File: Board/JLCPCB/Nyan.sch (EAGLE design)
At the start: 64 parts, among them Q1 8M, Q2 32768, U1 R-78C5.0-1.0, U3 A4988_STEP, U4 MAX6966, U5 ST3485, U6 74HCT541PW, U7 74HCT541PW, U8 STM32F10XCXT6, X1 WR-WTB2.0-2_THT-VER, X2 WR-WTB2.0-4_THT_VER, X3 WR-WTB2.0-5_THT-VER, X4 WR-WTB2.0-5_THT-VER, X6 68610614122, X7 68612414422, X8 68610414122

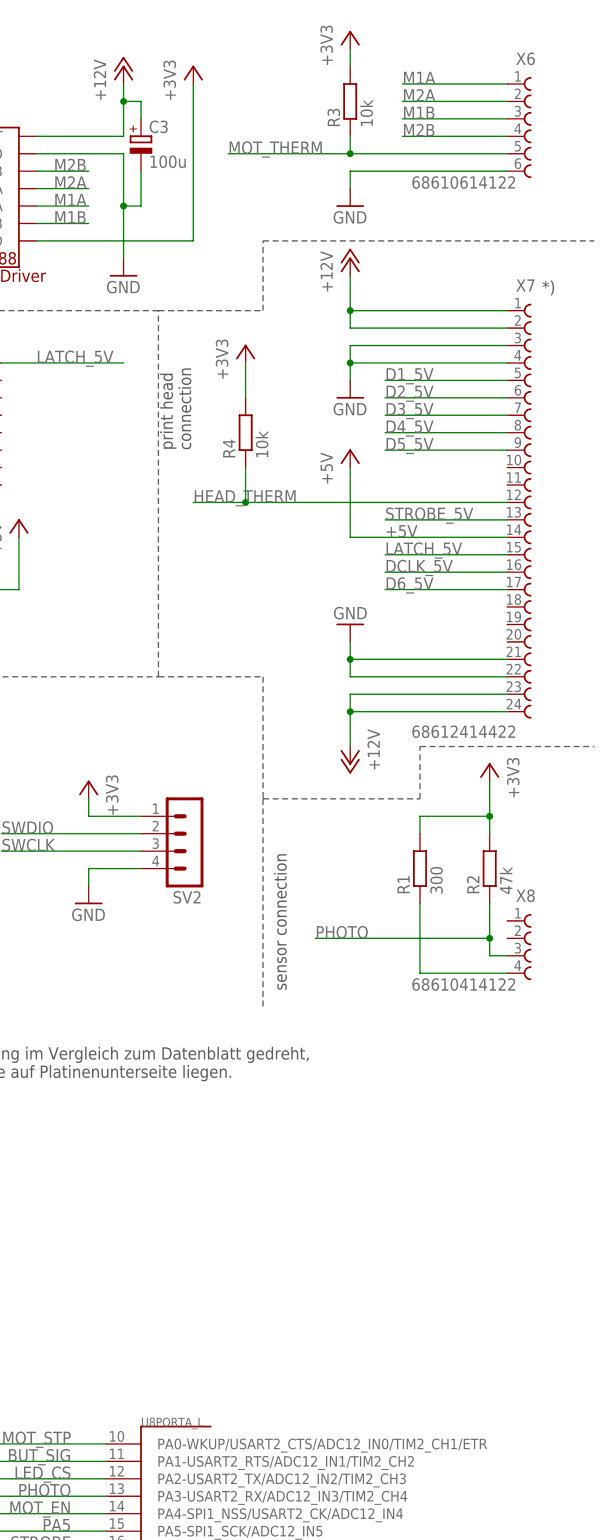
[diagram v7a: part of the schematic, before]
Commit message: [Board] Added debouncing circuitry for pushbutton
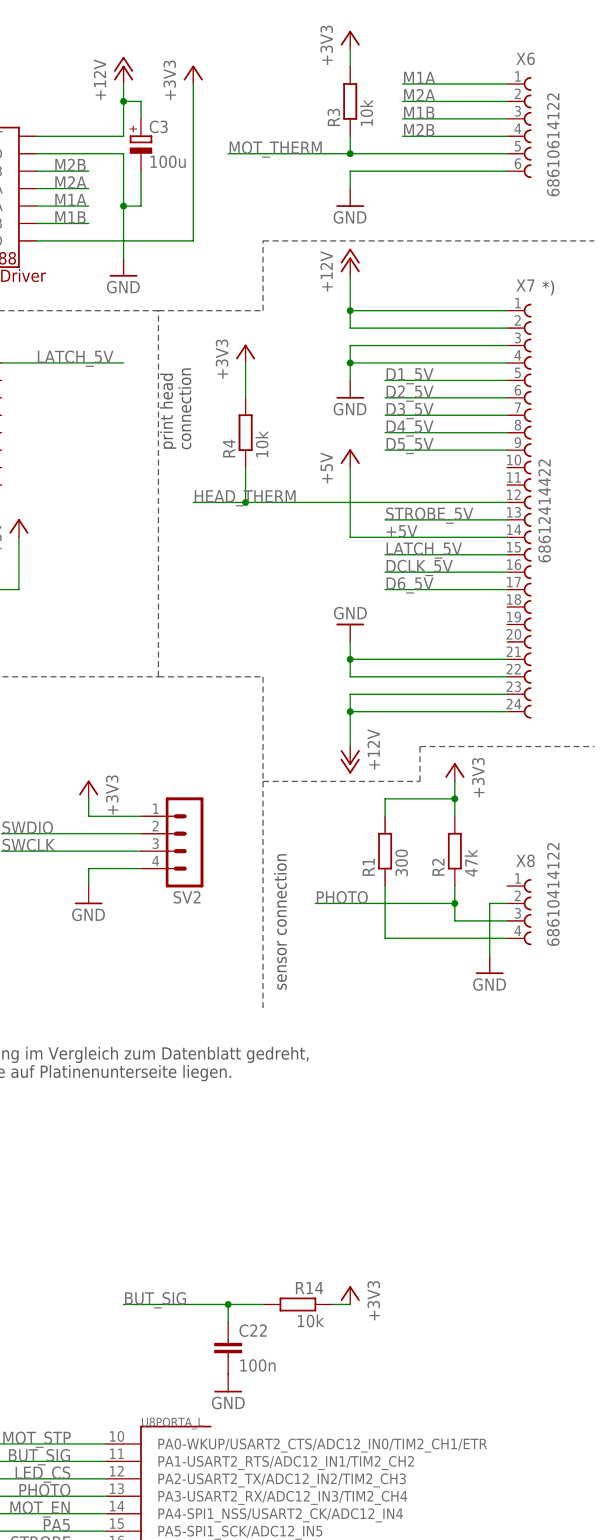
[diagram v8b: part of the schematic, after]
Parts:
- added C22: 100n, rcl:C-EUC0603
- added R14: 10k, rcl:R-EU_R0603
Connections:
- net +3V3: now also R14.1
- net BUT_SIG: now also C22.1, R14.2
- net GND: now also C22.2, X8.2
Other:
- moved on the sheet: R1, R2, X8
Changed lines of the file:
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@@
 <part name="+3V12" library="supply1" deviceset="+3V3" device=""/>
 <part name="+3V13" library="supply1" deviceset="+3V3" device=""/>
+<part name="GND23" library="supply1" deviceset="GND" device=""/>
+<part name="R14" library="rcl" deviceset="R-EU_" device="R0603" value="10k"/>
+<part name="C22" library="rcl" deviceset="C-EU" device="C0603" value="100n"/>
+<part name="+3V14" library="supply1" deviceset="+3V3" device=""/>
+<part name="GND24" library="supply1" deviceset="GND" device=""/>
 </parts>
 <sheets>
@@
 <wire x1="137.16" y1="137.16" x2="137.16" y2="142.24" width="0.1524" layer="97" style="longdash"/>
 <wire x1="200.66" y1="83.82" x2="215.9" y2="83.82" width="0.1524" layer="97" style="longdash"/>
-<wire x1="215.9" y1="83.82" x2="215.9" y2="66.04" width="0.1524" layer="97" style="longdash"/>
-<wire x1="215.9" y1="66.04" x2="215.9" y2="35.56" width="0.1524" layer="97" style="longdash"/>
+<wire x1="215.9" y1="83.82" x2="215.9" y2="68.58" width="0.1524" layer="97" style="longdash"/>
+<wire x1="215.9" y1="68.58" x2="215.9" y2="35.56" width="0.1524" layer="97" style="longdash"/>
 <wire x1="200.66" y1="137.16" x2="215.9" y2="137.16" width="0.1524" layer="97" style="longdash"/>
 <wire x1="215.9" y1="137.16" x2="215.9" y2="147.32" width="0.1524" layer="97" style="longdash"/>
 <wire x1="215.9" y1="147.32" x2="264.16" y2="147.32" width="0.1524" layer="97" style="longdash"/>
-<wire x1="215.9" y1="66.04" x2="238.76" y2="66.04" width="0.1524" layer="97" style="longdash"/>
-<wire x1="238.76" y1="66.04" x2="238.76" y2="73.66" width="0.1524" layer="97" style="longdash"/>
+<wire x1="215.9" y1="68.58" x2="238.76" y2="68.58" width="0.1524" layer="97" style="longdash"/>
+<wire x1="238.76" y1="68.58" x2="238.76" y2="73.66" width="0.1524" layer="97" style="longdash"/>
 <wire x1="238.76" y1="73.66" x2="264.16" y2="73.66" width="0.1524" layer="97" style="longdash"/>
 <wire x1="0" y1="-68.58" x2="78.74" y2="-68.58" width="0.1524" layer="97" style="longdash"/>
@@
 <instances>
 <instance part="U1" gate="G$1" x="43.18" y="170.18"/>
-<instance part="X8" gate="G$1" x="256.54" y="43.18" smashed="yes">
-<attribute name="NAME" x="252.73" y="51.038" size="1.778" layer="95"/>
-<attribute name="VALUE" x="237.49" y="38.1" size="1.778" layer="96"/>
+<instance part="X8" gate="G$1" x="256.54" y="48.26" smashed="yes">
+<attribute name="NAME" x="252.73" y="56.118" size="1.778" layer="95"/>
+<attribute name="VALUE" x="259.08" y="44.45" size="1.778" layer="96" rot="R90"/>
 </instance>
 <instance part="X6" gate="G$1" x="256.54" y="162.56" smashed="yes">
 <attribute name="NAME" x="252.73" y="172.958" size="1.778" layer="95"/>
-<attribute name="VALUE" x="237.49" y="154.94" size="1.778" layer="96"/>
+<attribute name="VALUE" x="259.08" y="153.67" size="1.778" layer="96" rot="R90"/>
 </instance>
 <instance part="X7" gate="G$1" x="256.54" y="109.22" smashed="yes">
 <attribute name="NAME" x="252.73" y="139.938" size="1.778" layer="95"/>
-<attribute name="VALUE" x="237.49" y="74.93" size="1.778" layer="96"/>
+<attribute name="VALUE" x="257.81" y="100.33" size="1.778" layer="96" rot="R90"/>
 </instance>
 <instance part="U3" gate="G$1" x="172.72" y="152.4"/>
@@
 <instance part="X5" gate="G$1" x="12.7" y="20.32"/>
 <instance part="GND9" gate="1" x="25.4" y="12.7"/>
-<instance part="R1" gate="G$1" x="238.76" y="55.88" rot="R90"/>
+<instance part="R1" gate="G$1" x="233.68" y="58.42" rot="R90"/>
 <instance part="P+9" gate="1" x="228.6" y="116.84"/>
 <instance part="P+10" gate="1" x="228.6" y="144.78"/>
-<instance part="R2" gate="G$1" x="248.92" y="55.88" rot="R90"/>
+<instance part="R2" gate="G$1" x="243.84" y="58.42" rot="R90"/>
 <instance part="GND10" gate="1" x="228.6" y="124.46"/>
 <instance part="P+11" gate="1" x="228.6" y="71.12" rot="R180"/>
@@
 <instance part="JP1" gate="A" x="33.02" y="-88.9" rot="R90"/>
 <instance part="JP2" gate="A" x="22.86" y="-88.9" rot="MR90"/>
-<instance part="+3V12" gate="G$1" x="248.92" y="71.12" rot="MR0"/>
+<instance part="+3V12" gate="G$1" x="243.84" y="71.12" rot="MR0"/>
 <instance part="+3V13" gate="G$1" x="213.36" y="132.08"/>
+<instance part="GND23" gate="1" x="248.92" y="40.64"/>
+<instance part="R14" gate="G$1" x="220.98" y="-7.62" rot="MR0"/>
+<instance part="C22" gate="G$1" x="210.82" y="-12.7"/>
+<instance part="+3V14" gate="G$1" x="228.6" y="-5.08" rot="MR0"/>
+<instance part="GND24" gate="1" x="210.82" y="-20.32" rot="MR0"/>
 </instances>
 <busses>
@@
 <pinref part="C19" gate="G$1" pin="1"/>
 </segment>
+<segment>
+<pinref part="X8" gate="G$1" pin="2"/>
+<pinref part="GND23" gate="1" pin="GND"/>
+<wire x1="251.46" y1="50.8" x2="248.92" y2="50.8" width="0.1524" layer="91"/>
+<wire x1="248.92" y1="50.8" x2="248.92" y2="43.18" width="0.1524" layer="91"/>
+</segment>
+<segment>
+<pinref part="GND24" gate="1" pin="GND"/>
+<pinref part="C22" gate="G$1" pin="2"/>
+</segment>
 </net>
 <net name="+12V" class="0">
@@
 <wire x1="193.04" y1="-30.48" x2="175.26" y2="-30.48" width="0.1524" layer="91"/>
 <label x="187.96" y="-30.48" size="1.778" layer="95" rot="MR0"/>
+</segment>
+<segment>
+<pinref part="R14" gate="G$1" pin="2"/>
+<wire x1="215.9" y1="-7.62" x2="210.82" y2="-7.62" width="0.1524" layer="91"/>
+<pinref part="C22" gate="G$1" pin="1"/>
+<wire x1="210.82" y1="-7.62" x2="195.58" y2="-7.62" width="0.1524" layer="91"/>
+<wire x1="210.82" y1="-10.16" x2="210.82" y2="-7.62" width="0.1524" layer="91"/>
+<junction x="210.82" y="-7.62"/>
+<label x="195.58" y="-7.62" size="1.778" layer="95"/>
 </segment>
 </net>
@@
 <segment>
 <pinref part="R1" gate="G$1" pin="2"/>
-<wire x1="248.92" y1="68.58" x2="248.92" y2="63.5" width="0.1524" layer="91"/>
+<wire x1="243.84" y1="68.58" x2="243.84" y2="66.04" width="0.1524" layer="91"/>
 <pinref part="R2" gate="G$1" pin="2"/>
-<wire x1="248.92" y1="63.5" x2="238.76" y2="63.5" width="0.1524" layer="91"/>
-<wire x1="238.76" y1="63.5" x2="238.76" y2="60.96" width="0.1524" layer="91"/>
-<wire x1="248.92" y1="63.5" x2="248.92" y2="60.96" width="0.1524" layer="91"/>
-<junction x="248.92" y="63.5"/>
+<wire x1="243.84" y1="66.04" x2="233.68" y2="66.04" width="0.1524" layer="91"/>
+<wire x1="233.68" y1="66.04" x2="233.68" y2="63.5" width="0.1524" layer="91"/>
+<wire x1="243.84" y1="66.04" x2="243.84" y2="63.5" width="0.1524" layer="91"/>
+<junction x="243.84" y="66.04"/>
 <pinref part="+3V12" gate="G$1" pin="+3V3"/>
 </segment>
@@
 <pinref part="+3V13" gate="G$1" pin="+3V3"/>
 <wire x1="213.36" y1="129.54" x2="213.36" y2="124.46" width="0.1524" layer="91"/>
+</segment>
+<segment>
+<pinref part="R14" gate="G$1" pin="1"/>
+<pinref part="+3V14" gate="G$1" pin="+3V3"/>
+<wire x1="226.06" y1="-7.62" x2="228.6" y2="-7.62" width="0.1524" layer="91"/>
 </segment>
 </net>
@@
 <segment>
 <pinref part="R2" gate="G$1" pin="1"/>
-<wire x1="248.92" y1="50.8" x2="248.92" y2="45.72" width="0.1524" layer="91"/>
-<wire x1="248.92" y1="45.72" x2="223.52" y2="45.72" width="0.1524" layer="91"/>
-<label x="223.52" y="45.72" size="1.778" layer="95"/>
+<wire x1="243.84" y1="53.34" x2="243.84" y2="50.8" width="0.1524" layer="91"/>
+<wire x1="243.84" y1="50.8" x2="223.52" y2="50.8" width="0.1524" layer="91"/>
+<label x="223.52" y="50.8" size="1.778" layer="95"/>
 <pinref part="X8" gate="G$1" pin="3"/>
-<wire x1="248.92" y1="45.72" x2="248.92" y2="43.18" width="0.1524" layer="91"/>
-<wire x1="248.92" y1="43.18" x2="251.46" y2="43.18" width="0.1524" layer="91"/>
-<junction x="248.92" y="45.72"/>
+<wire x1="243.84" y1="50.8" x2="243.84" y2="48.26" width="0.1524" layer="91"/>
+<wire x1="243.84" y1="48.26" x2="251.46" y2="48.26" width="0.1524" layer="91"/>
+<junction x="243.84" y="50.8"/>
 </segment>
 <segment>
@@
 <pinref part="R1" gate="G$1" pin="1"/>
 <pinref part="X8" gate="G$1" pin="4"/>
-<wire x1="238.76" y1="50.8" x2="238.76" y2="40.64" width="0.1524" layer="91"/>
-<wire x1="238.76" y1="40.64" x2="251.46" y2="40.64" width="0.1524" layer="91"/>
-</segment>
-</net>
+<wire x1="233.68" y1="53.34" x2="233.68" y2="45.72" width="0.1524" layer="91"/>
+<wire x1="233.68" y1="45.72" x2="251.46" y2="45.72" width="0.1524" layer="91"/>
+</segment>
+</net>
